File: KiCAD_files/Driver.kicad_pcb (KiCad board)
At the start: 2 copper layers, 90 x 40 mm, 38 parts, among them J1 Board_outline, U1 NMA1505SC, U12 SFH617A-2X009T, U3 UCC21520DW, U4 UCC21520DW

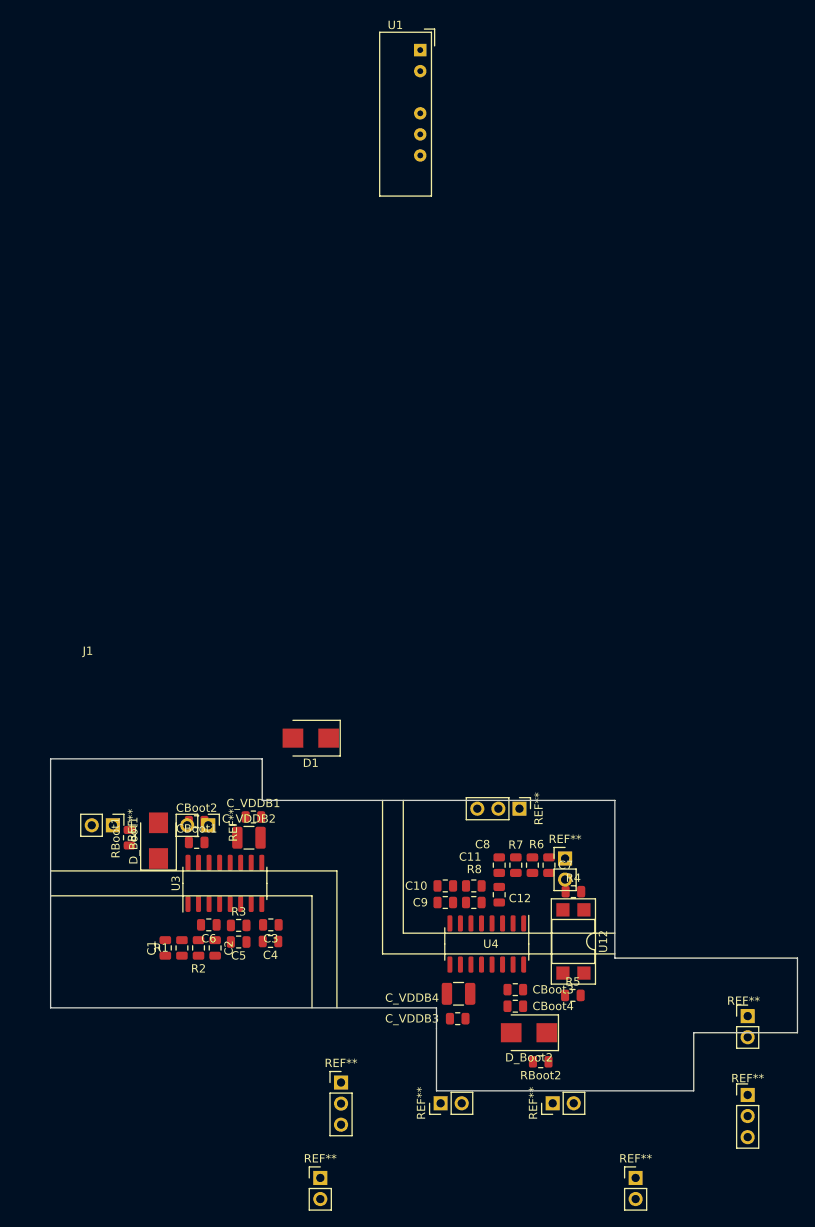
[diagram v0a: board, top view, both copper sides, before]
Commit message: Major modifications of the measurment board schematic Component placement finalized - 3D footprints added - mezzanine assembly on freecad added
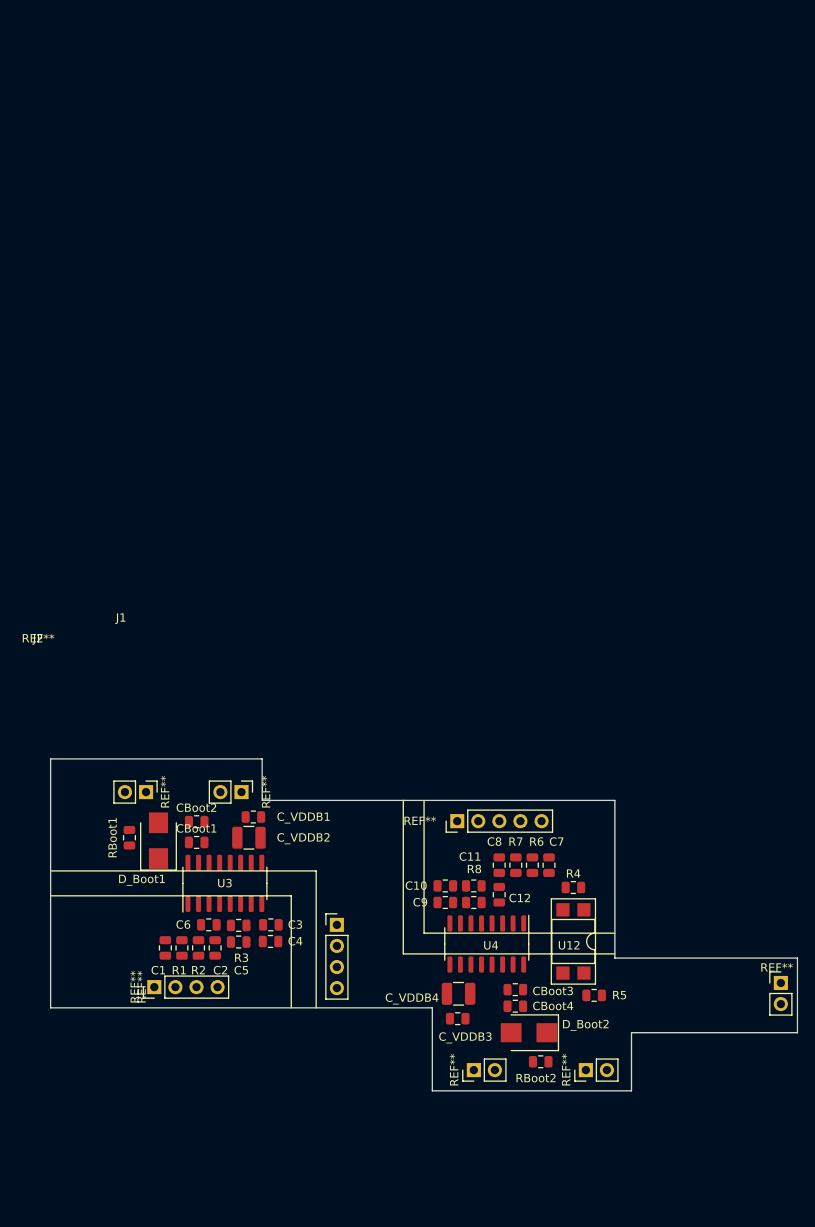
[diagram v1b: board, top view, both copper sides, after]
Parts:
- removed D1: D_TVS, Diode_SMD:D_SMB
- removed U1: NMA1505SC, Converter_DCDC:Converter_DCDC_muRata_NMAxxxxSC_THT
- added J2: Driver_stage_outline_inputs, Footprints:Driver_stage_outline_inputs, F.Cu at (29.0, 99.0)
- J1: value Board_outline -> Driver_stage_outline_outputs; footprint Footprints:Board outline -> Footprints:Driver_stage_outline_outputs
- moved J1 5.66 mm to (29.0, 99.0)
- moved R5 2.56 mm to (94.5, 139.5)
- moved R4 0.50 mm to (92.0, 126.5)
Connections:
- J1 pad 23: Net-(J1-Pad23) -> GNDREF
- R1 pad 1: /PWM_H1 -> /PWM_H1_D
- R2 pad 1: /PWM_L1 -> /PWM_L1_D
- R6 pad 1: /PWM_H2 -> /PWM_H2_D
- R7 pad 1: /PWM_L2 -> /PWM_L2_D
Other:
- outline, holes or cut-outs redrawn
